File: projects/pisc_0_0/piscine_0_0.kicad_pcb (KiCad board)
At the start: 2 copper layers, 23.4 x 34.7 mm, 17 parts, among them SW2 SW_Push, U1 ATmega328P-A

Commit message: added wizard silk-screen to pcb
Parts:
- added G***: LOGO, Library:wizard_silk_screen, F.Cu at (206.0, 72.0)

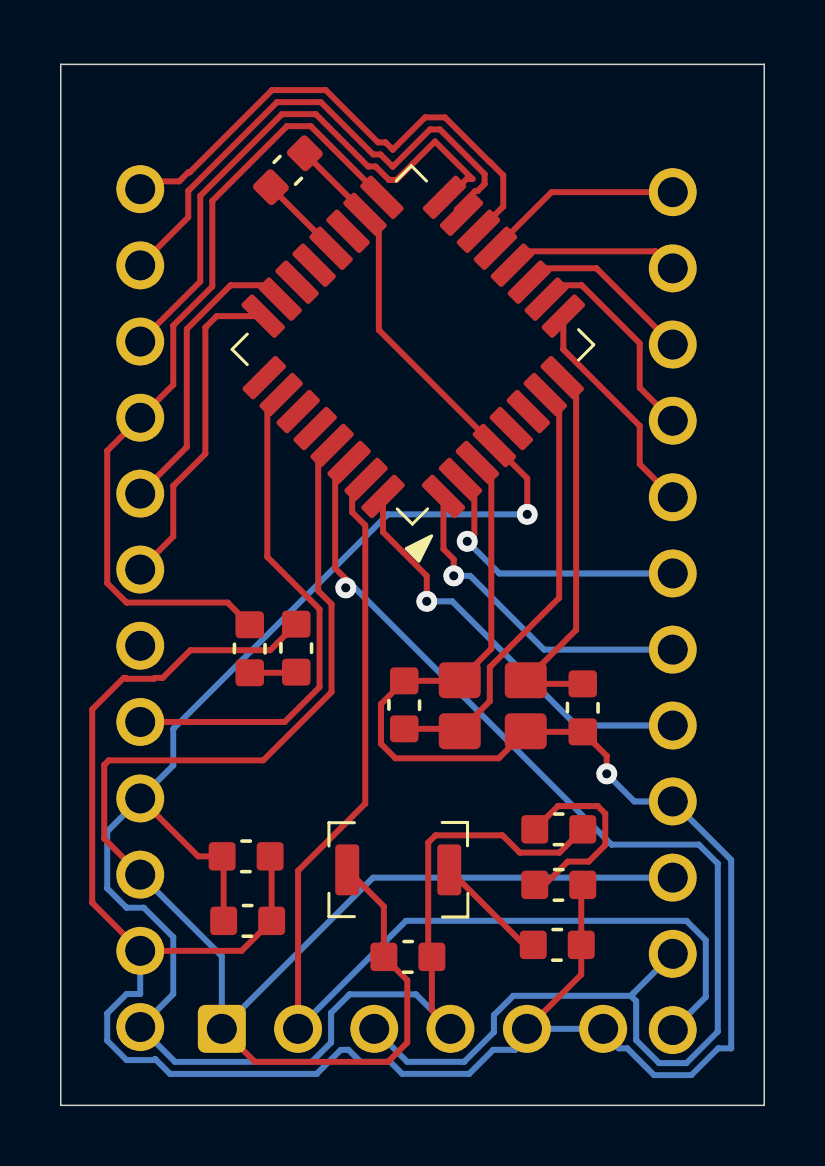
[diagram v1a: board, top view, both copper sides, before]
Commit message: added ground plane to pcb
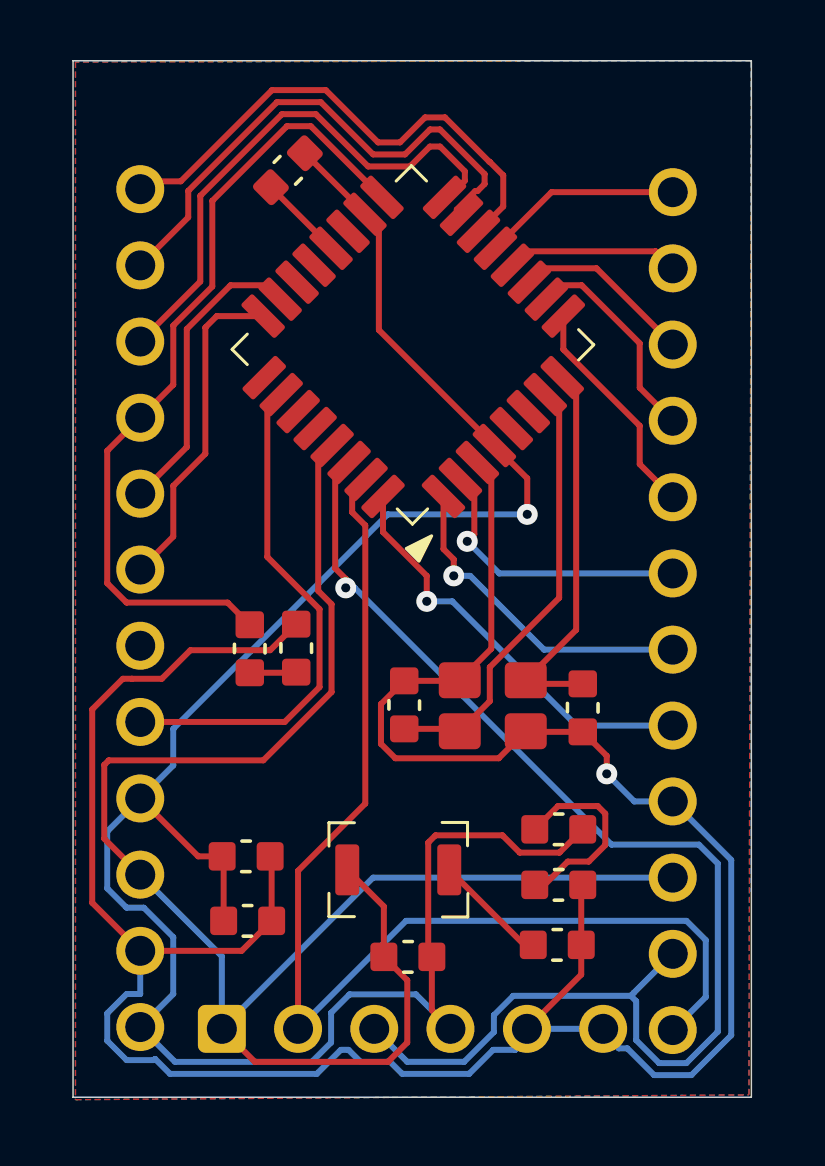
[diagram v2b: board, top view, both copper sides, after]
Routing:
- net MISO: track 19.1 -> 18.2 mm
- added copper zone on B.Cu, net GND
- added copper zone on F.Cu, net GND
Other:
- board size 23.4 x 34.7 mm -> 22.6 x 34.5 mm
